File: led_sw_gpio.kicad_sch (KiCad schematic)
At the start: 31 parts, among them Q6 2N7002, SW3 up, SW4 down, SW5 left, SW6 rigth, SW7 Switch_push, SW8 Switch_Push

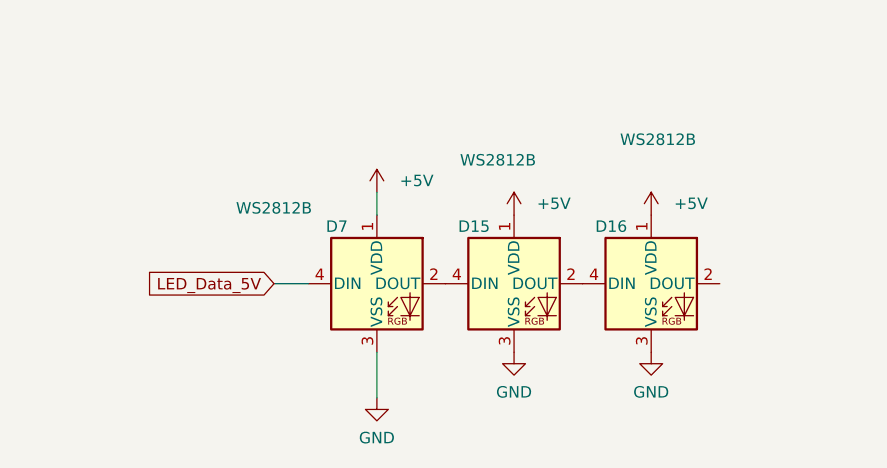
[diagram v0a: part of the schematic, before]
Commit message: Actualización de esquemas y PCB con datos LCSC y librerías JLC
- Añade propiedades LCSC a los símbolos de las hojas de esquema
- Actualiza las hojas TXS0108E, display, esp32_c6, ft232, inmp441,
  led_sw_gpio, max98357a, micro_sd, power_supply y el esquema raíz
- Reorganiza el PCB (footprints, jumpers y nets) y actualiza el proyecto
- Incluye las librerías locales JLCImport (símbolos, huellas y modelos 3D)
  y las entradas correspondientes en fp-lib-table y sym-lib-table
- Añade la documentación técnica en docs/ y el archivo de posiciones
  esp32_xiaozhi-all.pos
- Elimina los ZIP generados gebers.zip y production.zip
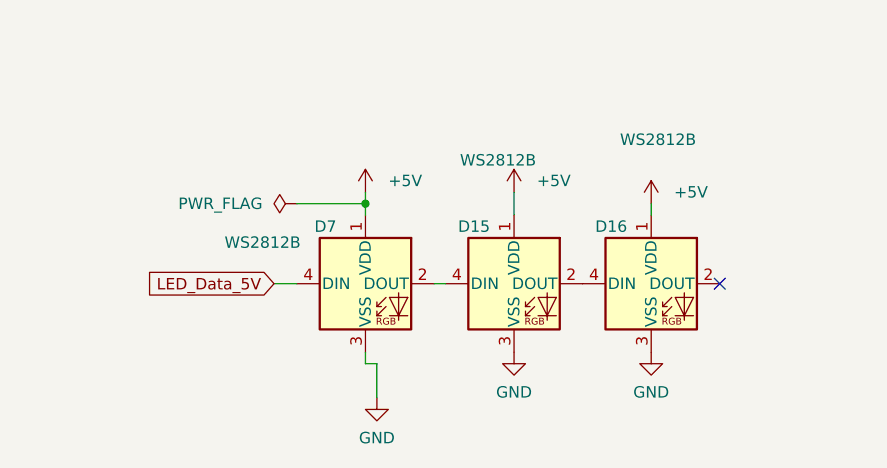
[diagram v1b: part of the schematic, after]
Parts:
- C24, C39, C40, C41, C42, C43, C44: LCSC (none) -> C1525
- D13: LCSC (none) -> C34499
- D15, D16, D7: LCSC (none) -> C2843785
- D3: LCSC (none) -> C2297
- D4: LCSC (none) -> C84256
- Q6: LCSC (none) -> C8545
- R27, R28, R31, R32, R33, R34, R35, R36, R39: LCSC (none) -> C4190
- R38, R40: LCSC (none) -> C17414
- SW3, SW4, SW5, SW6, SW7, SW8: LCSC (none) -> C2837531
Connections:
- no-connect marks 0 -> 1
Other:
- moved on the sheet: D7

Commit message: Actualización de esquemas, PCB y librerías
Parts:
- C24, C39, C40, C41, C42, C43, C44: LCSC C1525 -> C28233
- D4: value GREEN -> red
- R27, R28, R31, R32, R33, R34, R35, R36, R39: LCSC C4190 -> C17520
- SW3, SW4, SW5, SW6, SW7, SW8: footprint Button_Switch_SMD:SW_Push_1P1T_NO_CK_KSC9xxG -> kiC:SW_Push_1P1T_NO_6x6mm_H9.5mm; LCSC C2837531 -> C83916
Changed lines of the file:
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@@
 			)
 		)
-		(property "LCSC" "C4190"
+		(property "LCSC" "C17520"
 			(at 92.71 207.01 0)
 			(hide yes)
@@
 			)
 		)
-		(property "LCSC" "C4190"
+		(property "LCSC" "C17520"
 			(at 243.84 118.11 0)
 			(hide yes)
@@
 			)
 		)
-		(property "Footprint" "Button_Switch_SMD:SW_Push_1P1T_NO_CK_KSC9xxG"
+		(property "Footprint" "kiC:SW_Push_1P1T_NO_6x6mm_H9.5mm"
 			(at 151.13 147.32 0)
 			(hide yes)
@@
 			)
 		)
-		(property "LCSC" "C2837531"
+		(property "LCSC" "C83916"
 			(at 151.13 147.32 0)
 			(hide yes)
@@
 			)
 		)
-		(property "Value" "GREEN"
+		(property "Value" "red"
 			(at 96.52 189.992 0)
 			(show_name no)
@@
 			)
 		)
-		(property "LCSC" "C4190"
+		(property "LCSC" "C17520"
 			(at 176.53 115.57 0)
 			(hide yes)
@@
 			)
 		)
-		(property "Footprint" "Button_Switch_SMD:SW_Push_1P1T_NO_CK_KSC9xxG"
+		(property "Footprint" "kiC:SW_Push_1P1T_NO_6x6mm_H9.5mm"
 			(at 201.93 123.19 0)
 			(hide yes)
@@
 			)
 		)
-		(property "LCSC" "C2837531"
+		(property "LCSC" "C83916"
 			(at 201.93 123.19 0)
 			(hide yes)
@@
 			)
 		)
-		(property "LCSC" "C1525"
+		(property "LCSC" "C28233"
 			(at 186.69 127 0)
 			(hide yes)
@@
 			)
 		)
-		(property "LCSC" "C1525"
+		(property "LCSC" "C28233"
 			(at 245.11 209.55 0)
 			(hide yes)
@@
 			)
 		)
-		(property "LCSC" "C1525"
+		(property "LCSC" "C28233"
 			(at 234.95 147.32 0)
 			(hide yes)
@@
 			)
 		)
-		(property "LCSC" "C1525"
+		(property "LCSC" "C28233"
 			(at 137.16 151.13 0)
 			(hide yes)
@@
 			)
 		)
-		(property "LCSC" "C4190"
+		(property "LCSC" "C17520"
 			(at 187.96 115.57 0)
 			(hide yes)
@@
 			)
 		)
-		(property "LCSC" "C1525"
+		(property "LCSC" "C28233"
 			(at 243.84 134.62 0)
 			(hide yes)
@@
 			)
 		)
-		(property "LCSC" "C4190"
+		(property "LCSC" "C17520"
 			(at 125.73 120.65 0)
 			(hide yes)
@@
 			)
 		)
-		(property "LCSC" "C4190"
+		(property "LCSC" "C17520"
 			(at 138.43 120.65 0)
 			(hide yes)
@@
 			)
 		)
-		(property "Footprint" "Button_Switch_SMD:SW_Push_1P1T_NO_CK_KSC9xxG"
+		(property "Footprint" "kiC:SW_Push_1P1T_NO_6x6mm_H9.5mm"
 			(at 151.13 134.62 0)
 			(hide yes)
@@
 			)
 		)
-		(property "LCSC" "C2837531"
+		(property "LCSC" "C83916"
 			(at 151.13 134.62 0)
 			(hide yes)
@@
 			)
 		)
-		(property "Footprint" "Button_Switch_SMD:SW_Push_1P1T_NO_CK_KSC9xxG"
+		(property "Footprint" "kiC:SW_Push_1P1T_NO_6x6mm_H9.5mm"
 			(at 259.08 130.81 0)
 			(hide yes)
@@
 			)
 		)
-		(property "LCSC" "C2837531"
+		(property "LCSC" "C83916"
 			(at 259.08 130.81 0)
 			(hide yes)
@@
 			)
 		)
-		(property "LCSC" "C4190"
+		(property "LCSC" "C17520"
 			(at 234.95 118.11 0)
 			(hide yes)
@@
 			)
 		)
-		(property "LCSC" "C4190"
+		(property "LCSC" "C17520"
 			(at 82.55 207.01 0)
 			(hide yes)
@@
 			)
 		)
-		(property "Footprint" "Button_Switch_SMD:SW_Push_1P1T_NO_CK_KSC9xxG"
+		(property "Footprint" "kiC:SW_Push_1P1T_NO_6x6mm_H9.5mm"
 			(at 259.08 143.51 0)
 			(hide yes)
@@
 			)
 		)
-		(property "LCSC" "C2837531"
+		(property "LCSC" "C83916"
 			(at 259.08 143.51 0)
 			(hide yes)
@@
 			)
 		)
-		(property "LCSC" "C1525"
+		(property "LCSC" "C28233"
 			(at 139.7 138.43 0)
 			(hide yes)
@@
 			)
 		)
-		(property "LCSC" "C4190"
+		(property "LCSC" "C17520"
 			(at 105.41 207.01 0)
 			(hide yes)
@@
 			)
 		)
-		(property "LCSC" "C1525"
+		(property "LCSC" "C28233"
 			(at 177.8 139.7 0)
 			(hide yes)
@@
 			)
 		)
-		(property "Footprint" "Button_Switch_SMD:SW_Push_1P1T_NO_CK_KSC9xxG"
+		(property "Footprint" "kiC:SW_Push_1P1T_NO_6x6mm_H9.5mm"
 			(at 201.93 135.89 0)
 			(hide yes)
@@
 			)
 		)
-		(property "LCSC" "C2837531"
+		(property "LCSC" "C83916"
 			(at 201.93 135.89 0)
 			(hide yes)

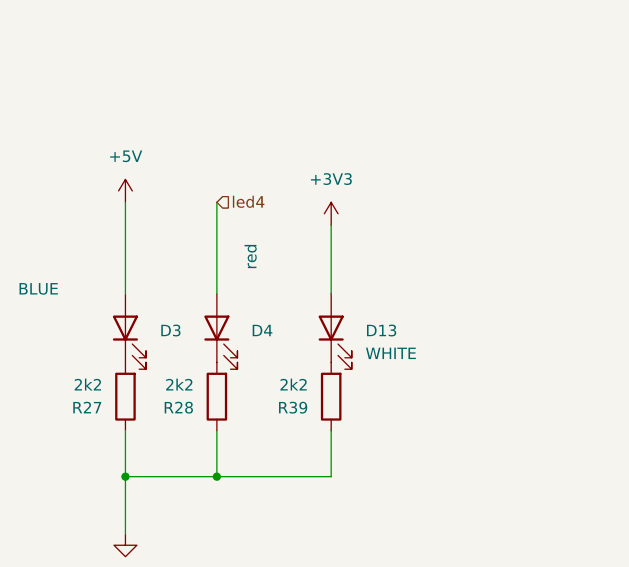
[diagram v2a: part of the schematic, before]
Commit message: correccion de numero de partes de componentes
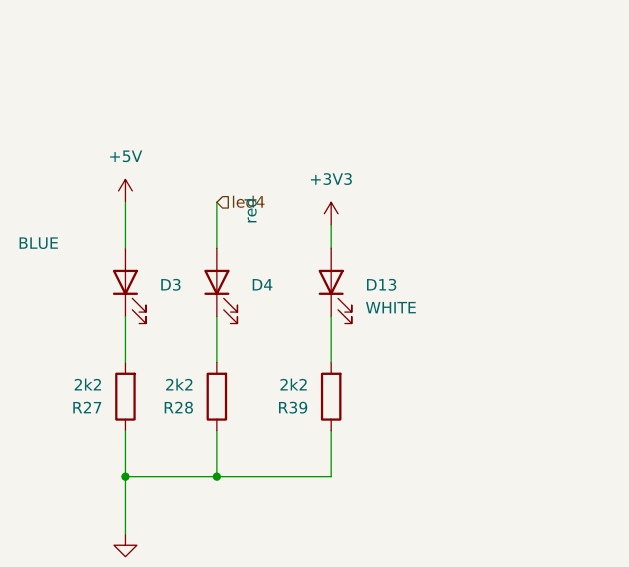
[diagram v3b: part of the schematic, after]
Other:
- moved on the sheet: D13, D3, D4
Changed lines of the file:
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@@
 	(wire
 		(pts
+			(xy 92.71 198.12) (xy 92.71 203.2)
+		)
+		(stroke
+			(width 0)
+			(type default)
+		)
+	)
+	(wire
+		(pts
 			(xy 92.71 215.9) (xy 105.41 215.9)
 		)
@@
 	(wire
 		(pts
-			(xy 105.41 187.96) (xy 105.41 195.58)
+			(xy 105.41 187.96) (xy 105.41 190.5)
 		)
 		(stroke
@@
 	(wire
 		(pts
-			(xy 82.55 195.58) (xy 82.55 185.42)
+			(xy 82.55 190.5) (xy 82.55 185.42)
+		)
+		(stroke
+			(width 0)
+			(type default)
+		)
+	)
+	(wire
+		(pts
+			(xy 105.41 198.12) (xy 105.41 203.2)
 		)
 		(stroke
@@
 	(wire
 		(pts
-			(xy 92.71 195.58) (xy 92.71 185.42)
+			(xy 92.71 190.5) (xy 92.71 185.42)
 		)
 		(stroke
@@
 	(wire
 		(pts
+			(xy 82.55 198.12) (xy 82.55 203.2)
+		)
+		(stroke
+			(width 0)
+			(type default)
+		)
+	)
+	(wire
+		(pts
 			(xy 234.95 101.6) (xy 234.95 114.3)
 		)
@@
 	(symbol
 		(lib_id "Device:LED")
-		(at 92.71 199.39 90)
+		(at 92.71 194.31 90)
 		(unit 1)
 		(body_style 1)
@@
 		(dnp no)
 		(property "Reference" "D4"
-			(at 96.52 199.7074 90)
+			(at 96.52 194.6274 90)
 			(show_name no)
 			(do_not_autoplace no)
@@
 		)
 		(property "Value" "red"
-			(at 96.52 189.992 0)
+			(at 96.52 184.912 0)
 			(show_name no)
 			(do_not_autoplace no)
@@
 		)
 		(property "Footprint" "Diode_SMD:D_0805_2012Metric"
-			(at 92.71 199.39 0)
+			(at 92.71 194.31 0)
 			(hide yes)
 			(show_name no)
@@
 		)
 		(property "Datasheet" ""
-			(at 92.71 199.39 0)
+			(at 92.71 194.31 0)
 			(hide yes)
 			(show_name no)
@@
 		)
 		(property "Description" "Light emitting diode green"
-			(at 92.71 199.39 0)
+			(at 92.71 194.31 0)
 			(hide yes)
 			(show_name no)
@@
 		)
 		(property "Sim.Pins" "1=K 2=A"
-			(at 92.71 199.39 0)
+			(at 92.71 194.31 0)
 			(hide yes)
 			(show_name no)
@@
 		)
 		(property "LCSC" "C84256"
-			(at 92.71 199.39 90)
+			(at 92.71 194.31 90)
 			(hide yes)
 			(show_name no)
@@
 	(symbol
 		(lib_id "Device:LED")
-		(at 105.41 199.39 90)
+		(at 105.41 194.31 90)
 		(unit 1)
 		(body_style 1)
@@
 		(fields_autoplaced yes)
 		(property "Reference" "D13"
-			(at 109.22 199.7074 90)
+			(at 109.22 194.6274 90)
 			(show_name no)
 			(do_not_autoplace no)
@@
 		)
 		(property "Value" "WHITE"
-			(at 109.22 202.2474 90)
+			(at 109.22 197.1674 90)
 			(show_name no)
 			(do_not_autoplace no)
@@
 		)
 		(property "Footprint" "Diode_SMD:D_0805_2012Metric"
-			(at 105.41 199.39 0)
+			(at 105.41 194.31 0)
 			(hide yes)
 			(show_name no)
@@
 		)
 		(property "Datasheet" ""
-			(at 105.41 199.39 0)
+			(at 105.41 194.31 0)
 			(hide yes)
 			(show_name no)
@@
 		)
 		(property "Description" "Light emitting diode white"
-			(at 105.41 199.39 0)
+			(at 105.41 194.31 0)
 			(hide yes)
 			(show_name no)
@@
 		)
 		(property "Sim.Pins" "1=K 2=A"
-			(at 105.41 199.39 0)
+			(at 105.41 194.31 0)
 			(hide yes)
 			(show_name no)
@@
 		)
 		(property "LCSC" "C34499"
-			(at 105.41 199.39 90)
+			(at 105.41 194.31 90)
 			(hide yes)
 			(show_name no)
@@
 	(symbol
 		(lib_id "Device:LED")
-		(at 82.55 199.39 90)
+		(at 82.55 194.31 90)
 		(unit 1)
 		(body_style 1)
@@
 		(dnp no)
 		(property "Reference" "D3"
-			(at 86.36 199.7074 90)
+			(at 86.36 194.6274 90)
 			(show_name no)
 			(do_not_autoplace no)
@@
 		)
 		(property "Value" "BLUE"
-			(at 70.612 195.072 90)
+			(at 70.612 189.992 90)
 			(show_name no)
 			(do_not_autoplace no)
@@
 		)
 		(property "Footprint" "Diode_SMD:D_0805_2012Metric"
-			(at 82.55 199.39 0)
+			(at 82.55 194.31 0)
 			(hide yes)
 			(show_name no)
@@
 		)
 		(property "Datasheet" ""
-			(at 82.55 199.39 0)
+			(at 82.55 194.31 0)
 			(hide yes)
 			(show_name no)
@@
 		)
 		(property "Description" "Light emitting diode blue"
-			(at 82.55 199.39 0)
+			(at 82.55 194.31 0)
 			(hide yes)
 			(show_name no)
@@
 		)
 		(property "Sim.Pins" "1=K 2=A"
-			(at 82.55 199.39 0)
+			(at 82.55 194.31 0)
 			(hide yes)
 			(show_name no)
@@
 		)
 		(property "LCSC" "C2297"
-			(at 82.55 199.39 90)
+			(at 82.55 194.31 90)
 			(hide yes)
 			(show_name no)

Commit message: correccion de partes
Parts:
- D15, D16, D7: value WS2812B -> XL-5050RGBC-2812B; LCSC Part # C2761795 -> C2843785
- SW3: value up -> K2-1102SP-A4SC-04; footprint kiC:SW_Push_1P1T_NO_6x6mm_H9.5mm -> Button_Switch_SMD:SW_SPST_PTS645Sx43SMTR92
- SW4: value down -> K2-1102SP-A4SC-04; footprint kiC:SW_Push_1P1T_NO_6x6mm_H9.5mm -> Button_Switch_SMD:SW_SPST_PTS645Sx43SMTR92
- SW5: value left -> K2-1102SP-A4SC-04; footprint kiC:SW_Push_1P1T_NO_6x6mm_H9.5mm -> Button_Switch_SMD:SW_SPST_PTS645Sx43SMTR92
- SW6: value rigth -> K2-1102SP-A4SC-04; footprint kiC:SW_Push_1P1T_NO_6x6mm_H9.5mm -> Button_Switch_SMD:SW_SPST_PTS645Sx43SMTR92
- SW7: value Switch_push -> K2-1102SP-A4SC-04; footprint kiC:SW_Push_1P1T_NO_6x6mm_H9.5mm -> Button_Switch_SMD:SW_SPST_PTS645Sx43SMTR92; LCSC C83916 -> C83916
- SW8: value Switch_Push -> K2-1102SP-A4SC-04; footprint kiC:SW_Push_1P1T_NO_6x6mm_H9.5mm -> Button_Switch_SMD:SW_SPST_PTS645Sx43SMTR92; LCSC C83916 -> C83916
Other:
- moved on the sheet: C43
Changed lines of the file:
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@@
 	)
 	(junction
-		(at 273.05 143.51)
-		(diameter 0)
-		(color 0 0 0 0)
-	)
-	(junction
 		(at 297.18 189.23)
 		(diameter 0)
@@
 	)
 	(junction
-		(at 234.95 143.51)
-		(diameter 0)
-		(color 0 0 0 0)
-	)
-	(junction
 		(at 125.73 105.41)
 		(diameter 0)
@@
 	)
 	(junction
+		(at 273.05 143.51)
+		(diameter 0)
+		(color 0 0 0 0)
+	)
+	(junction
 		(at 139.7 134.62)
 		(diameter 0)
 		(color 0 0 0 0)
 	)
+	(junction
+		(at 234.95 143.51)
+		(diameter 0)
+		(color 0 0 0 0)
+	)
 	(no_connect
 		(at 186.69 247.65)
@@
 	(wire
 		(pts
+			(xy 234.95 168.91) (xy 234.95 166.37)
+		)
+		(stroke
+			(width 0)
+			(type default)
+		)
+	)
+	(wire
+		(pts
+			(xy 234.95 158.75) (xy 234.95 143.51)
+		)
+		(stroke
+			(width 0)
+			(type default)
+		)
+	)
+	(wire
+		(pts
 			(xy 125.73 105.41) (xy 125.73 116.84)
 		)
@@
 	(wire
 		(pts
-			(xy 273.05 154.94) (xy 273.05 143.51)
+			(xy 273.05 170.18) (xy 273.05 143.51)
 		)
 		(stroke
@@
 			)
 		)
-		(property "Value" "down"
+		(property "Value" "K2-1102SP-A4SC-04"
 			(at 151.13 142.24 0)
 			(show_name no)
@@
 			)
 		)
-		(property "Footprint" "kiC:SW_Push_1P1T_NO_6x6mm_H9.5mm"
+		(property "Footprint" "Button_Switch_SMD:SW_SPST_PTS645Sx43SMTR92"
 			(at 151.13 147.32 0)
 			(hide yes)
@@
 	(symbol
 		(lib_id "power:GND")
-		(at 234.95 151.13 0)
+		(at 234.95 168.91 0)
 		(unit 1)
 		(body_style 1)
@@
 		(fields_autoplaced yes)
 		(property "Reference" "#PWR0116"
-			(at 234.95 157.48 0)
+			(at 234.95 175.26 0)
 			(hide yes)
 			(show_name no)
@@
 		)
 		(property "Value" "GND"
-			(at 234.95 156.21 0)
+			(at 234.95 173.99 0)
 			(show_name no)
 			(do_not_autoplace no)
@@
 		)
 		(property "Footprint" ""
-			(at 234.95 151.13 0)
+			(at 234.95 168.91 0)
 			(hide yes)
 			(show_name no)
@@
 		)
 		(property "Datasheet" ""
-			(at 234.95 151.13 0)
+			(at 234.95 168.91 0)
 			(hide yes)
 			(show_name no)
@@
 		)
 		(property "Description" ""
-			(at 234.95 151.13 0)
+			(at 234.95 168.91 0)
 			(show_name no)
 			(do_not_autoplace no)
@@
 			)
 		)
-		(property "Value" "left"
+		(property "Value" "K2-1102SP-A4SC-04"
 			(at 201.93 118.11 0)
 			(show_name no)
@@
 			)
 		)
-		(property "Footprint" "kiC:SW_Push_1P1T_NO_6x6mm_H9.5mm"
+		(property "Footprint" "Button_Switch_SMD:SW_SPST_PTS645Sx43SMTR92"
 			(at 201.93 123.19 0)
 			(hide yes)
@@
 		(lib_name "C_1")
 		(lib_id "Device:C")
-		(at 234.95 147.32 0)
+		(at 234.95 162.56 0)
 		(unit 1)
 		(body_style 1)
@@
 		(fields_autoplaced yes)
 		(property "Reference" "C43"
-			(at 238.76 146.05 0)
+			(at 238.76 161.29 0)
 			(show_name no)
 			(do_not_autoplace no)
@@
 		)
 		(property "Value" "100nf"
-			(at 238.76 148.59 0)
+			(at 238.76 163.83 0)
 			(show_name no)
 			(do_not_autoplace no)
@@
 		)
 		(property "Footprint" "Capacitor_SMD:C_0805_2012Metric"
-			(at 235.9152 151.13 0)
+			(at 235.9152 166.37 0)
 			(hide yes)
 			(show_name no)
@@
 		)
 		(property "Datasheet" ""
-			(at 234.95 147.32 0)
+			(at 234.95 162.56 0)
 			(hide yes)
 			(show_name no)
@@
 		)
 		(property "Description" ""
-			(at 234.95 147.32 0)
+			(at 234.95 162.56 0)
 			(show_name no)
 			(do_not_autoplace no)
@@
 		)
 		(property "LCSC" "C28233"
-			(at 234.95 147.32 0)
+			(at 234.95 162.56 0)
 			(hide yes)
 			(show_name no)
@@
 			)
 		)
-		(property "Value" "up"
+		(property "Value" "K2-1102SP-A4SC-04"
 			(at 151.13 129.54 0)
 			(show_name no)
@@
 			)
 		)
-		(property "Footprint" "kiC:SW_Push_1P1T_NO_6x6mm_H9.5mm"
+		(property "Footprint" "Button_Switch_SMD:SW_SPST_PTS645Sx43SMTR92"
 			(at 151.13 134.62 0)
 			(hide yes)
@@
 			)
 		)
-		(property "Value" "Switch_push"
+		(property "Value" "K2-1102SP-A4SC-04"
 			(at 259.08 125.73 0)
 			(show_name no)
@@
 			)
 		)
-		(property "Footprint" "kiC:SW_Push_1P1T_NO_6x6mm_H9.5mm"
+		(property "Footprint" "Button_Switch_SMD:SW_SPST_PTS645Sx43SMTR92"
 			(at 259.08 130.81 0)
 			(hide yes)
@@
 			)
 		)
-		(property "LCSC" "C83916"
+		(property "LCSC" " C83916"
 			(at 259.08 130.81 0)
 			(hide yes)
@@
 	(symbol
 		(lib_id "power:GND")
-		(at 273.05 154.94 0)
+		(at 273.05 170.18 0)
 		(unit 1)
 		(body_style 1)
@@
 		(fields_autoplaced yes)
 		(property "Reference" "#PWR060"
-			(at 273.05 161.29 0)
+			(at 273.05 176.53 0)
 			(hide yes)
 			(show_name no)
@@
 		)
 		(property "Value" "GND"
-			(at 273.05 160.02 0)
+			(at 273.05 175.26 0)
 			(show_name no)
 			(do_not_autoplace no)
@@
 		)
 		(property "Footprint" ""
-			(at 273.05 154.94 0)
+			(at 273.05 170.18 0)
 			(hide yes)
 			(show_name no)
@@
 		)
 		(property "Datasheet" ""
-			(at 273.05 154.94 0)
+			(at 273.05 170.18 0)
 			(hide yes)
 			(show_name no)
@@
 		)
 		(property "Description" ""
-			(at 273.05 154.94 0)
+			(at 273.05 170.18 0)
 			(show_name no)
 			(do_not_autoplace no)
@@
 			)
 		)
-		(property "Value" "WS2812B"
-			(at 135.89 243.078 0)
+		(property "Value" "XL-5050RGBC-2812B"
+			(at 131.572 257.556 0)
 			(show_name no)
 			(do_not_autoplace no)
@@
 		)
 		(property "Footprint" "LED_SMD:LED_WS2812B_PLCC4_5.0x5.0mm_P3.2mm"
-			(at 148.59 255.27 0)
-			(hide yes)
+			(at 111.252 269.24 0)
 			(show_name no)
 			(do_not_autoplace no)
@@
 			)
 		)
-		(property "LCSC Part #" "C2761795"
+		(property "LCSC Part #" "C2843785"
 			(at 147.32 247.65 0)
 			(hide yes)
@@
 			)
 		)
-		(property "Value" "WS2812B"
+		(property "Value" "XL-5050RGBC-2812B"
 			(at 179.832 231.648 0)
 			(show_name no)
@@
 			)
 		)
-		(property "LCSC Part #" "C2761795"
+		(property "LCSC Part #" "C2843785"
 			(at 179.07 247.65 0)
 			(hide yes)
@@
 			)
 		)
-		(property "Value" "Switch_Push"
+		(property "Value" "K2-1102SP-A4SC-04"
 			(at 259.08 138.43 0)
 			(show_name no)
@@
 			)
 		)
-		(property "Footprint" "kiC:SW_Push_1P1T_NO_6x6mm_H9.5mm"
+		(property "Footprint" "Button_Switch_SMD:SW_SPST_PTS645Sx43SMTR92"
 			(at 259.08 143.51 0)
 			(hide yes)
@@
 			)
 		)
-		(property "LCSC" "C83916"
+		(property "LCSC" " C83916"
 			(at 259.08 143.51 0)
 			(hide yes)
@@
 			)
 		)
-		(property "Value" "WS2812B"
+		(property "Value" "XL-5050RGBC-2812B"
 			(at 162.052 233.934 0)
 			(show_name no)
@@
 			)
 		)
-		(property "LCSC Part #" "C2761795"
+		(property "LCSC Part #" "C2843785"
 			(at 163.83 247.65 0)
 			(hide yes)
@@
 			)
 		)
-		(property "Value" "rigth"
+		(property "Value" "K2-1102SP-A4SC-04"
 			(at 201.93 130.81 0)
 			(show_name no)
@@
 			)
 		)
-		(property "Footprint" "kiC:SW_Push_1P1T_NO_6x6mm_H9.5mm"
+		(property "Footprint" "Button_Switch_SMD:SW_SPST_PTS645Sx43SMTR92"
 			(at 201.93 135.89 0)
 			(hide yes)
